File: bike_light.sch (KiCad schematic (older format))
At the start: 0 parts

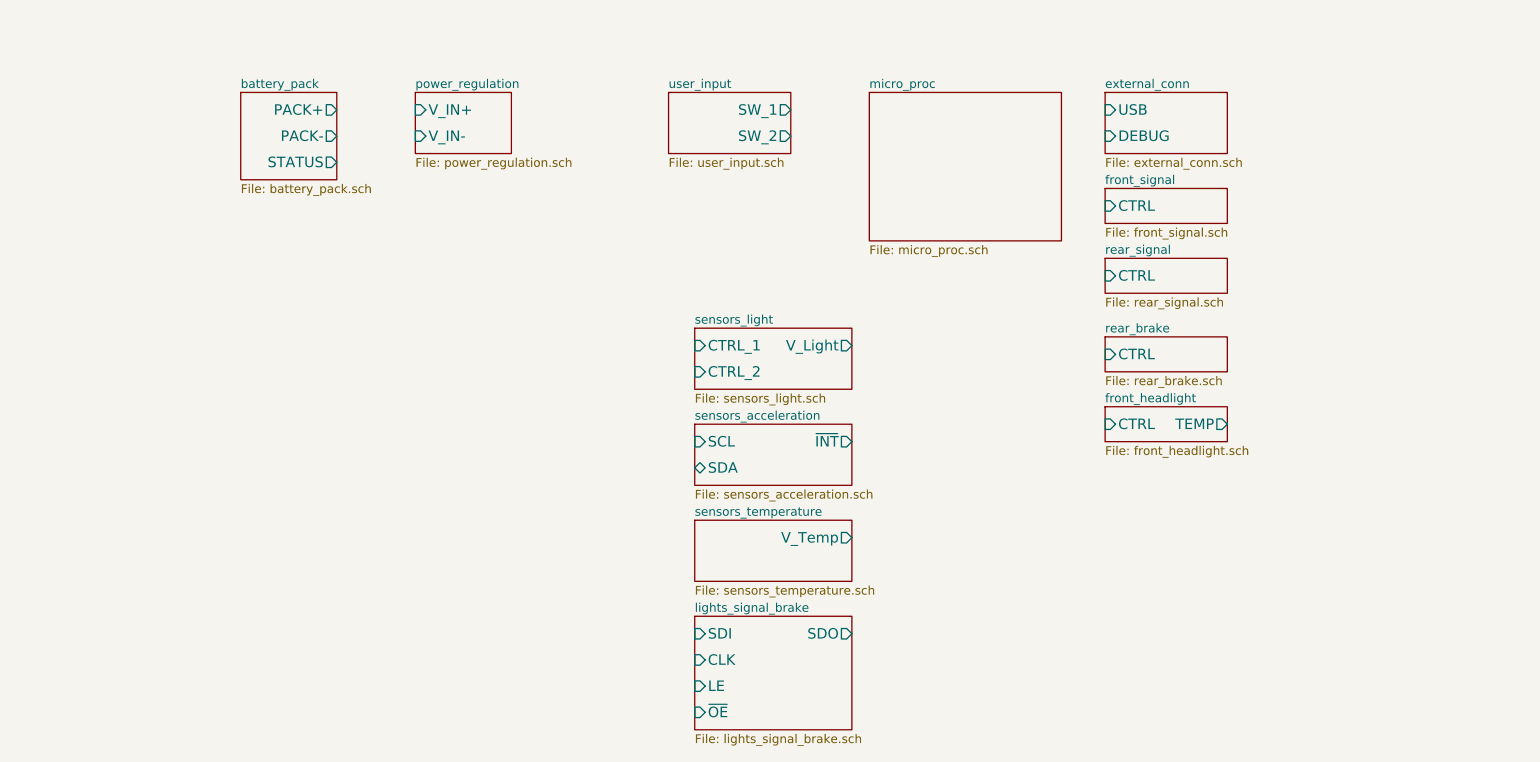
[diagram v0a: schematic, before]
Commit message: Various components added
USB conn, general outputs, brake signal, touch sensor
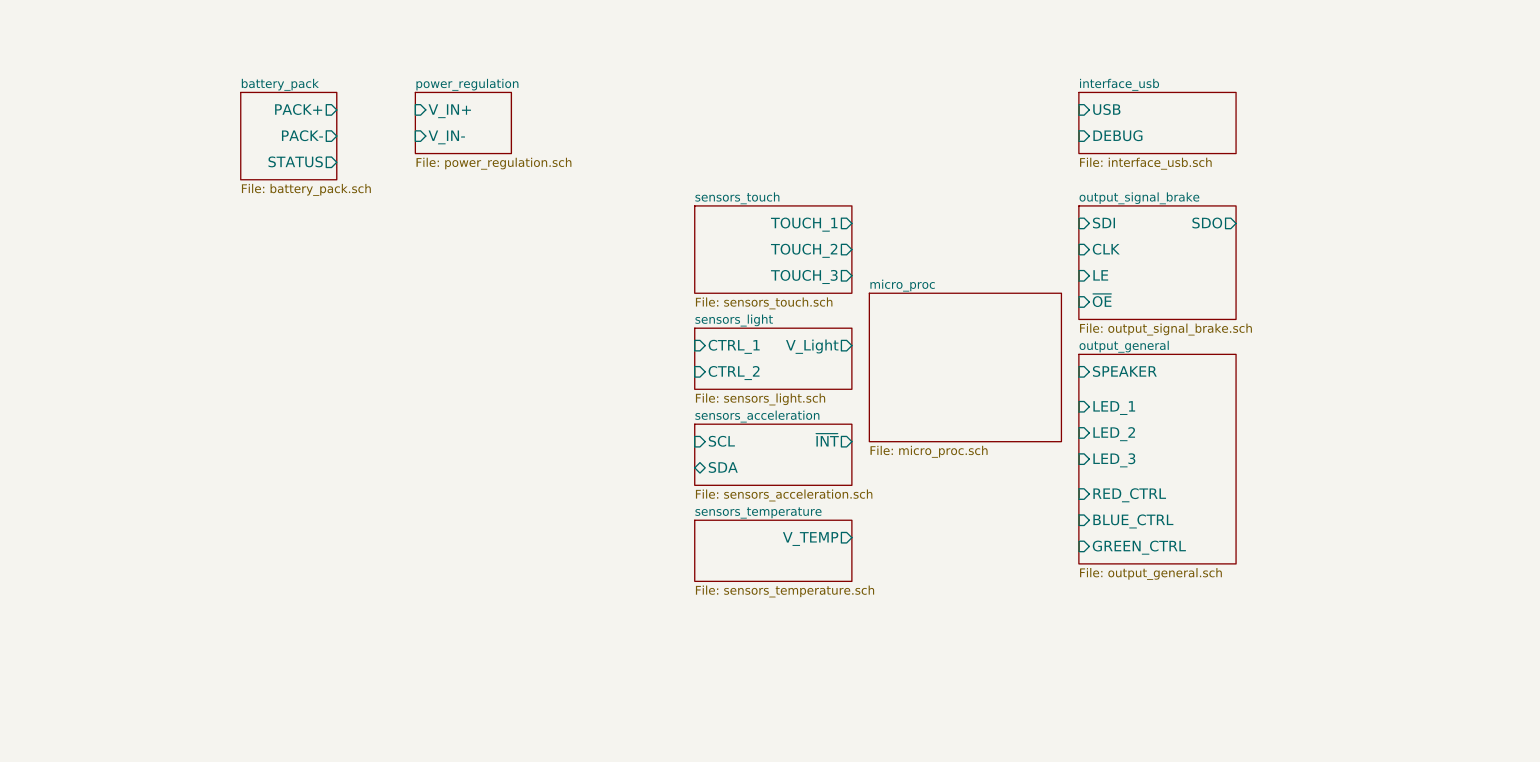
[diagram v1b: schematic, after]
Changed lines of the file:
@@
 $Descr USLetter 11000 8500
 encoding utf-8
-Sheet 1 14
+Sheet 1 11
 Title "Bike Light"
-Date "10 nov 2013"
+Date "11 nov 2013"
 Rev "1.0"
 Comp ""
@@
 $EndSheet
 $Sheet
-S 5500 1100 1100 850
+S 5500 2250 1100 850
 U 5224C543
 F0 "micro_proc" 50
@@
 $EndSheet
 $Sheet
-S 4350 1100 700  350
-U 5224C574
-F0 "user_input" 50
-F1 "user_input.sch" 50
-F2 "SW_1" O R 5050 1200 60
-F3 "SW_2" O R 5050 1350 60
-$EndSheet
-$Sheet
-S 6850 1100 700  350
+S 6700 1100 900  350
 U 5224C595
-F0 "external_conn" 50
-F1 "external_conn.sch" 50
-F2 "USB" I L 6850 1200 60
-F3 "DEBUG" I L 6850 1350 60
-$EndSheet
-$Sheet
-S 6850 2500 700  200
-U 5224C62E
-F0 "rear_brake" 50
-F1 "rear_brake.sch" 50
-F2 "CTRL" I L 6850 2600 60
-$EndSheet
-$Sheet
-S 6850 2050 700  200
-U 5224C648
-F0 "rear_signal" 50
-F1 "rear_signal.sch" 50
-F2 "CTRL" I L 6850 2150 60
-$EndSheet
-$Sheet
-S 6850 2900 700  200
-U 5224C659
-F0 "front_headlight" 50
-F1 "front_headlight.sch" 50
-F2 "CTRL" I L 6850 3000 60
-F3 "TEMP" O R 7550 3000 60
-$EndSheet
-$Sheet
-S 6850 1650 700  200
-U 5224C605
-F0 "front_signal" 50
-F1 "front_signal.sch" 50
-F2 "CTRL" I L 6850 1750 60
+F0 "interface_usb" 50
+F1 "interface_usb.sch" 50
+F2 "USB" I L 6700 1200 60
+F3 "DEBUG" I L 6700 1350 60
 $EndSheet
 $Sheet
@@
 F0 "sensors_temperature" 50
 F1 "sensors_temperature.sch" 50
-F2 "V_Temp" O R 5400 3650 60
+F2 "V_TEMP" O R 5400 3650 60
 $EndSheet
 $Sheet
@@
 $EndSheet
 $Sheet
-S 4500 4100 900  650
+S 6700 1750 900  650
 U 527F3E83
-F0 "lights_signal_brake" 50
-F1 "lights_signal_brake.sch" 50
-F2 "SDI" I L 4500 4200 60
-F3 "CLK" I L 4500 4350 60
-F4 "LE" I L 4500 4500 60
-F5 "~OE" I L 4500 4650 60
-F6 "SDO" O R 5400 4200 60
+F0 "output_signal_brake" 50
+F1 "output_signal_brake.sch" 50
+F2 "SDI" I L 6700 1850 60
+F3 "CLK" I L 6700 2000 60
+F4 "LE" I L 6700 2150 60
+F5 "~OE" I L 6700 2300 60
+F6 "SDO" O R 7600 1850 60
+$EndSheet
+$Sheet
+S 4500 1750 900  500
+U 527FE989
+F0 "sensors_touch" 50
+F1 "sensors_touch.sch" 50
+F2 "TOUCH_1" O R 5400 1850 60
+F3 "TOUCH_2" O R 5400 2000 60
+F4 "TOUCH_3" O R 5400 2150 60
+$EndSheet
+$Sheet
+S 6700 2600 900  1200
+U 528029D1
+F0 "output_general" 50
+F1 "output_general.sch" 50
+F2 "SPEAKER" I L 6700 2700 60
+F3 "LED_1" I L 6700 2900 60
+F4 "LED_2" I L 6700 3050 60
+F5 "LED_3" I L 6700 3200 60
+F6 "RED_CTRL" I L 6700 3400 60
+F7 "BLUE_CTRL" I L 6700 3550 60
+F8 "GREEN_CTRL" I L 6700 3700 60
 $EndSheet
 $EndSCHEMATC

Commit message: Battery management stuff
:D
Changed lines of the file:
@@
 $Descr USLetter 11000 8500
 encoding utf-8
-Sheet 1 11
+Sheet 1 14
 Title "Bike Light"
-Date "11 nov 2013"
+Date "12 nov 2013"
 Rev "1.0"
 Comp ""
@@
 $EndDescr
 $Sheet
-S 1900 1100 550  500
+S 2450 1650 1000 350
 U 5224C457
 F0 "battery_pack" 50
 F1 "battery_pack.sch" 50
-F2 "PACK+" O R 2450 1200 60
-F3 "PACK-" O R 2450 1350 60
-F4 "STATUS" O R 2450 1500 60
+F2 "V_PACK" O R 3450 1750 60
+F3 "V_PACK_BUFFERED" O R 3450 1900 60
 $EndSheet
 $Sheet
-S 2900 1100 550  350
+S 3850 850  550  350
 U 5224C4FA
 F0 "power_regulation" 50
 F1 "power_regulation.sch" 50
-F2 "V_IN-" I L 2900 1350 60
-F3 "V_IN+" I L 2900 1200 60
+F2 "V_IN-" I L 3850 1100 60
+F3 "V_IN+" I L 3850 950 60
 $EndSheet
 $Sheet
@@
 $EndSheet
 $Sheet
-S 4500 3550 900  350
+S 4500 3550 900  200
 U 527B19B4
 F0 "sensors_temperature" 50

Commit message: random minor thing
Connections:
- wire segments 0 -> 32
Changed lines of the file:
@@
 Sheet 1 14
 Title "Bike Light"
-Date "12 nov 2013"
+Date "15 nov 2013"
 Rev "1.0"
 Comp ""
@@
 $EndSheet
 $Sheet
-S 5500 2250 1100 850
+S 5500 1750 1100 2350
 U 5224C543
 F0 "micro_proc" 50
@@
 $EndSheet
 $Sheet
-S 6700 1100 900  350
+S 6700 750  900  350
 U 5224C595
 F0 "interface_usb" 50
 F1 "interface_usb.sch" 50
-F2 "USB" I L 6700 1200 60
-F3 "DEBUG" I L 6700 1350 60
+F2 "USB" I L 6700 850 60
+F3 "DEBUG" I L 6700 1000 60
 $EndSheet
 $Sheet
-S 4500 3550 900  200
+S 4500 3750 900  200
 U 527B19B4
 F0 "sensors_temperature" 50
 F1 "sensors_temperature.sch" 50
-F2 "V_TEMP" O R 5400 3650 60
+F2 "V_TEMP" O R 5400 3850 60
 $EndSheet
 $Sheet
-S 4500 2450 900  350
+S 4500 2550 900  350
 U 527B1CA6
 F0 "sensors_light" 50
 F1 "sensors_light.sch" 50
-F2 "V_Light" O R 5400 2550 60
-F3 "CTRL_1" I L 4500 2550 60
-F4 "CTRL_2" I L 4500 2700 60
+F2 "V_Light" O R 5400 2650 60
+F3 "CTRL_1" I L 4500 2650 60
+F4 "CTRL_2" I L 4500 2800 60
 $EndSheet
 $Sheet
-S 4500 3000 900  350
+S 4500 3200 900  350
 U 527C7E4B
 F0 "sensors_acceleration" 50
 F1 "sensors_acceleration.sch" 50
-F2 "SCL" I L 4500 3100 60
-F3 "SDA" B L 4500 3250 60
-F4 "~INT" O R 5400 3100 60
+F2 "SCL" I L 4500 3300 60
+F3 "SDA" B L 4500 3450 60
+F4 "~INT" O R 5400 3300 60
 $EndSheet
 $Sheet
@@
 F8 "GREEN_CTRL" I L 6700 3700 60
 $EndSheet
+Wire Wire Line
+	5400 1850 5500 1850
+Wire Wire Line
+	5400 2000 5500 2000
+Wire Wire Line
+	5400 2150 5500 2150
+Wire Wire Line
+	4500 2650 4450 2650
+Wire Wire Line
+	4450 2650 4450 2450
+Wire Wire Line
+	4450 2450 5500 2450
+Wire Wire Line
+	4500 2800 4350 2800
+Wire Wire Line
+	4350 2800 4350 2350
+Wire Wire Line
+	4350 2350 5500 2350
+Wire Wire Line
+	5400 2650 5500 2650
+Wire Wire Line
+	4500 3300 4450 3300
+Wire Wire Line
+	4450 3300 4450 3100
+Wire Wire Line
+	4450 3100 5500 3100
+Wire Wire Line
+	4500 3450 4350 3450
+Wire Wire Line
+	4350 3450 4350 3000
+Wire Wire Line
+	4350 3000 5500 3000
+Wire Wire Line
+	5400 3300 5500 3300
+Wire Wire Line
+	5400 3850 5500 3850
+Wire Wire Line
+	6600 1850 6700 1850
+Wire Wire Line
+	6700 2000 6600 2000
+Wire Wire Line
+	6700 2150 6600 2150
+Wire Wire Line
+	6700 2300 6600 2300
+Wire Wire Line
+	7600 1850 7850 1850
+Wire Wire Line
+	7850 1850 7850 2500
+Wire Wire Line
+	7850 2500 6600 2500
+Wire Wire Line
+	6700 2700 6600 2700
+Wire Wire Line
+	6700 2900 6600 2900
+Wire Wire Line
+	6700 3050 6600 3050
+Wire Wire Line
+	6700 3200 6600 3200
+Wire Wire Line
+	6700 3400 6600 3400
+Wire Wire Line
+	6700 3550 6600 3550
+Wire Wire Line
+	6700 3700 6600 3700
 $EndSCHEMATC

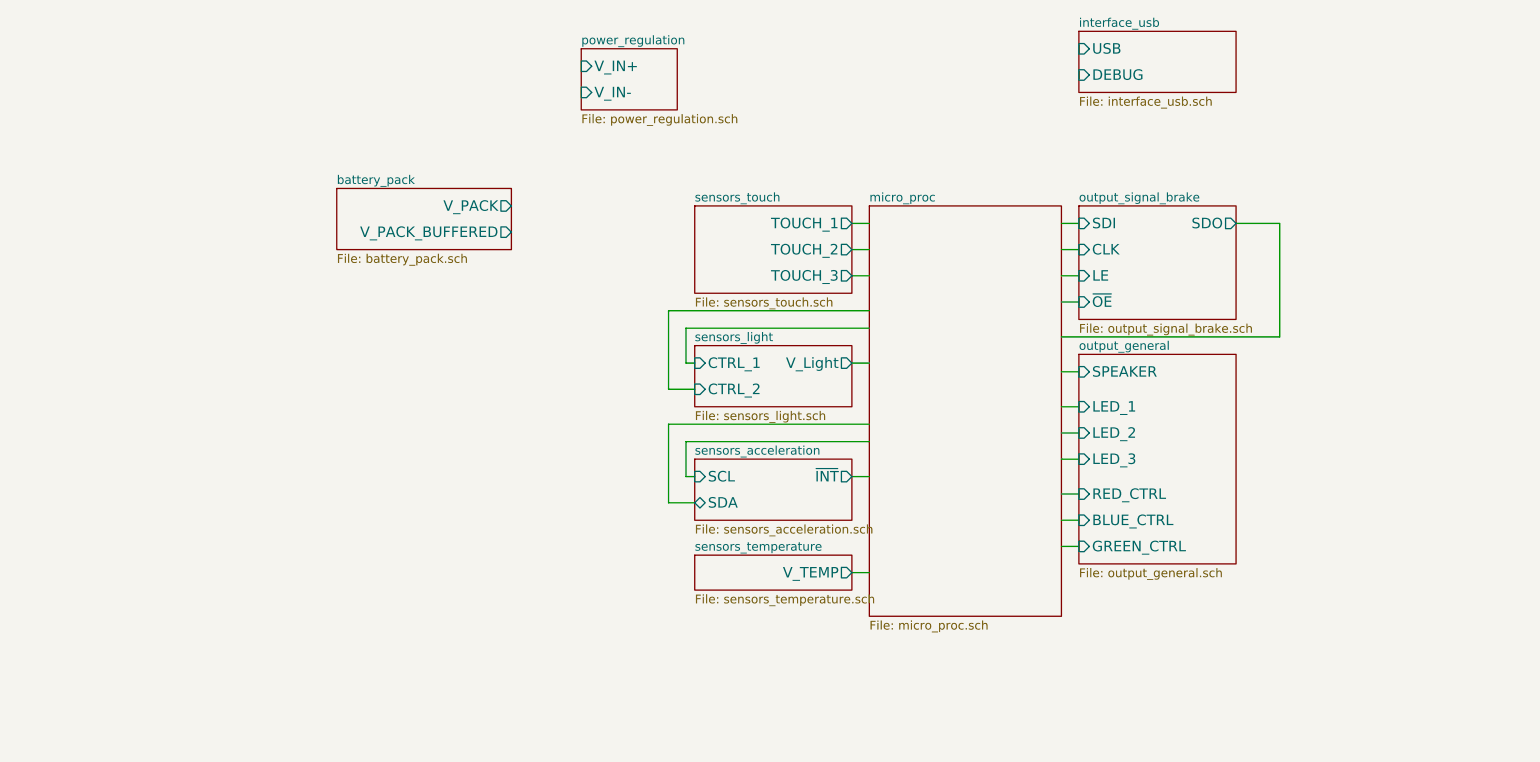
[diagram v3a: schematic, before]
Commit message: Added comments to schematic
shows what needs to be done
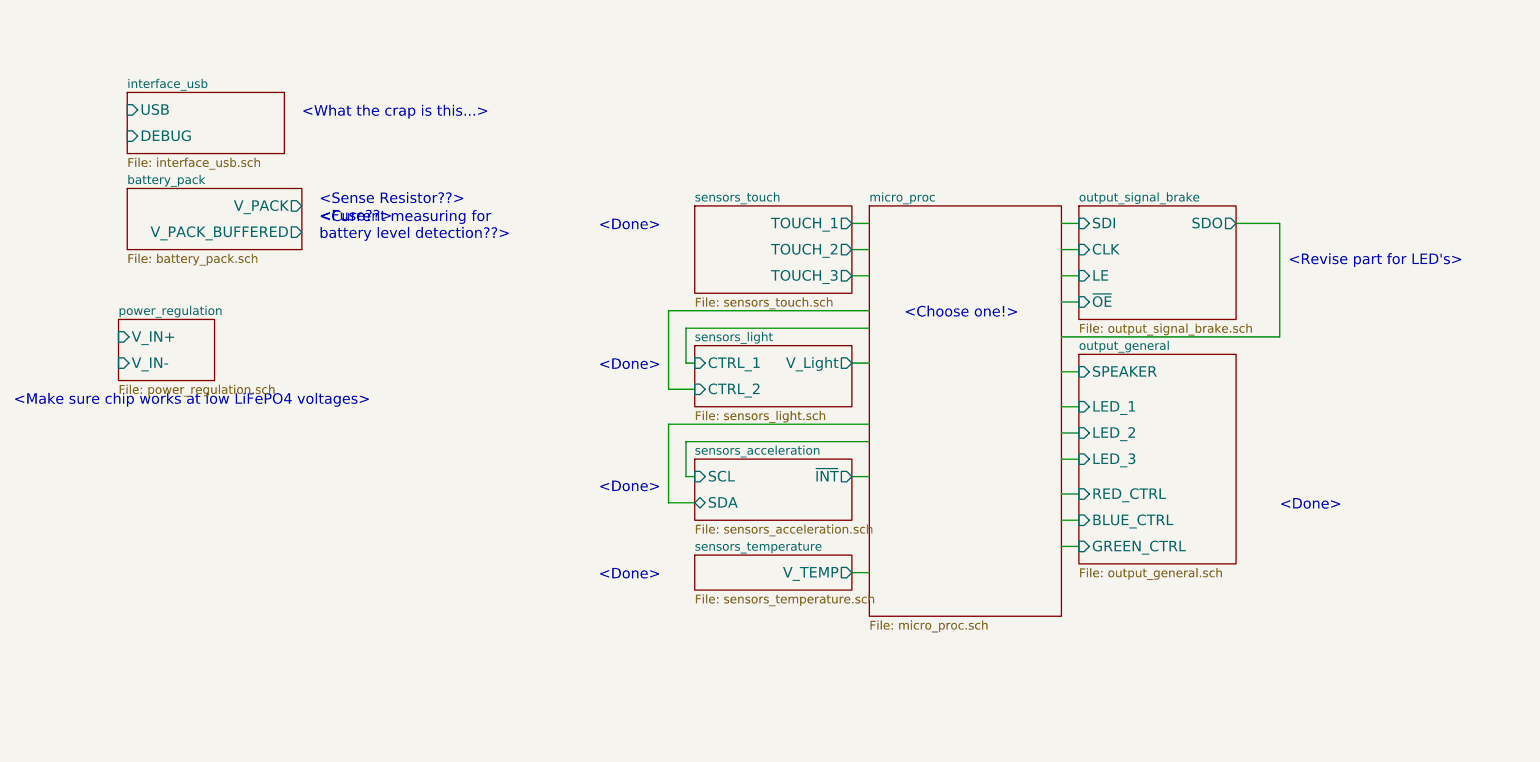
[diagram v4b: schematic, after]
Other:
- note added: "<Choose one!>"
- note added: "<Current measuring for \nbattery level detection??>"
- note added: "<Done>"
- note added: "<Fuse??>"
- note added: "<Make sure chip works at low LiFePO4 voltages>"
- note added: "<Revise part for LED's>"
- note added: "<Sense Resistor??>"
- note added: "<What the crap is this...>"
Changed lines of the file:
@@
 Sheet 1 14
 Title "Bike Light"
-Date "15 nov 2013"
+Date "17 nov 2013"
 Rev "1.0"
 Comp ""
@@
 $EndDescr
 $Sheet
-S 2450 1650 1000 350
+S 1250 1650 1000 350
 U 5224C457
 F0 "battery_pack" 50
 F1 "battery_pack.sch" 50
-F2 "V_PACK" O R 3450 1750 60
-F3 "V_PACK_BUFFERED" O R 3450 1900 60
+F2 "V_PACK" O R 2250 1750 60
+F3 "V_PACK_BUFFERED" O R 2250 1900 60
 $EndSheet
 $Sheet
-S 3850 850  550  350
+S 1200 2400 550  350
 U 5224C4FA
 F0 "power_regulation" 50
 F1 "power_regulation.sch" 50
-F2 "V_IN-" I L 3850 1100 60
-F3 "V_IN+" I L 3850 950 60
+F2 "V_IN-" I L 1200 2650 60
+F3 "V_IN+" I L 1200 2500 60
 $EndSheet
 $Sheet
@@
 $EndSheet
 $Sheet
-S 6700 750  900  350
+S 1250 1100 900  350
 U 5224C595
 F0 "interface_usb" 50
 F1 "interface_usb.sch" 50
-F2 "USB" I L 6700 850 60
-F3 "DEBUG" I L 6700 1000 60
+F2 "USB" I L 1250 1200 60
+F3 "DEBUG" I L 1250 1350 60
 $EndSheet
 $Sheet
@@
 Wire Wire Line
 	6700 3700 6600 3700
+Text Notes 3950 1900 0    60   ~ 0
+<Done>
+Text Notes 3950 2700 0    60   ~ 0
+<Done>
+Text Notes 3950 3900 0    60   ~ 0
+<Done>
+Text Notes 7850 3500 0    60   ~ 0
+<Done>
+Text Notes 7900 2100 0    60   ~ 0
+<Revise part for LED's>
+Text Notes 5700 2400 0    60   ~ 0
+<Choose one!>
+Text Notes 3950 3400 0    60   ~ 0
+<Done>
+Text Notes 2350 1750 0    60   ~ 0
+<Sense Resistor??>
+Text Notes 2350 1850 0    60   ~ 0
+<Fuse??>
+Text Notes 2350 1950 0    60   ~ 0
+<Current measuring for \nbattery level detection??>
+Text Notes 2250 1250 0    60   ~ 0
+<What the crap is this...>
+Text Notes 600  2900 0    60   ~ 0
+<Make sure chip works at low LiFePO4 voltages>
 $EndSCHEMATC

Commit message: revised LED parts to match reality
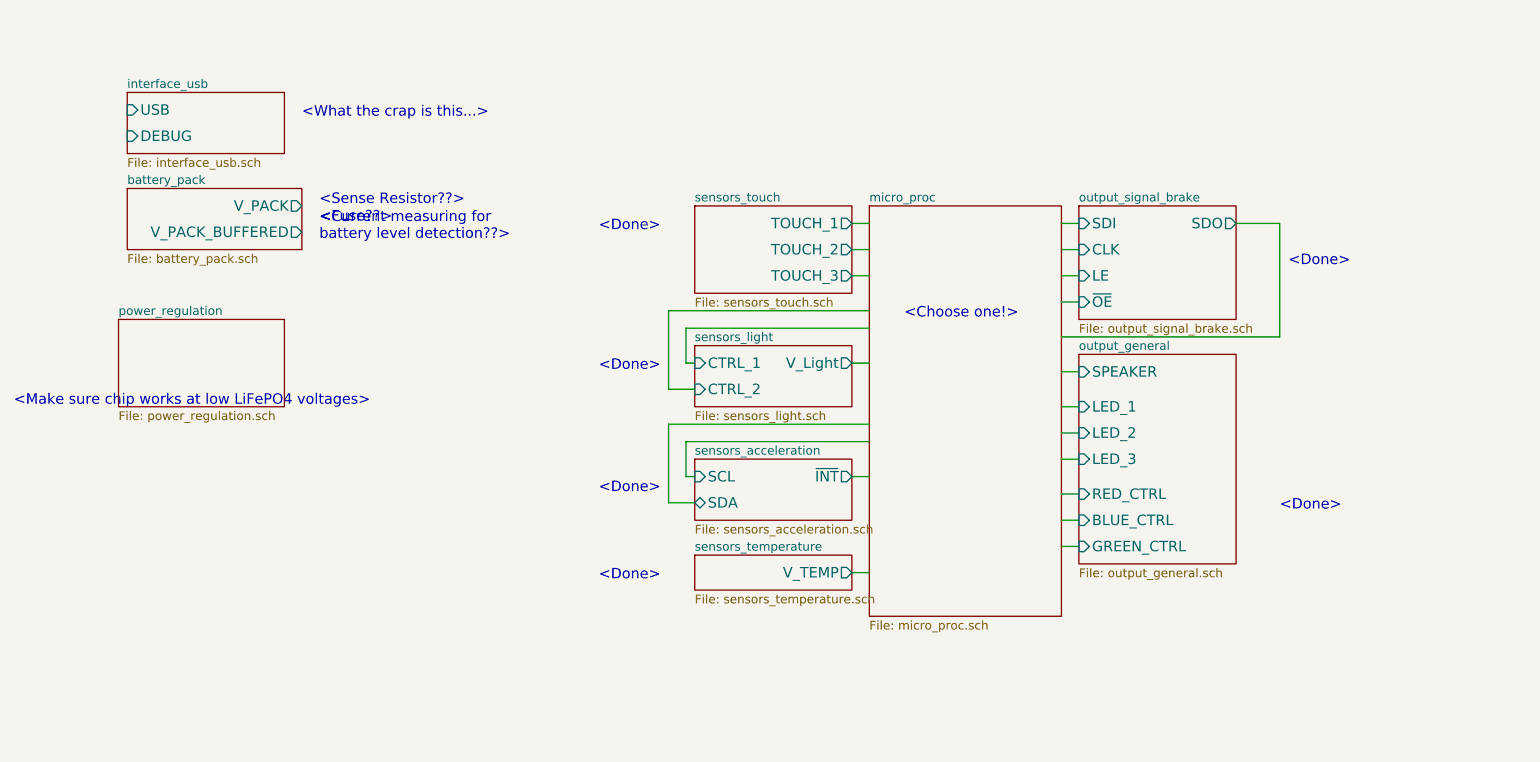
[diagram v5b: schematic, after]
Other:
- note removed: "<Revise part for LED's>"
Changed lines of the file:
@@
 Sheet 1 14
 Title "Bike Light"
-Date "17 nov 2013"
+Date "18 nov 2013"
 Rev "1.0"
 Comp ""
@@
 $EndSheet
 $Sheet
-S 1200 2400 550  350
+S 1200 2400 950  500
 U 5224C4FA
 F0 "power_regulation" 50
 F1 "power_regulation.sch" 50
-F2 "V_IN-" I L 1200 2650 60
-F3 "V_IN+" I L 1200 2500 60
 $EndSheet
 $Sheet
@@
 <Done>
 Text Notes 7900 2100 0    60   ~ 0
-<Revise part for LED's>
+<Done>
 Text Notes 5700 2400 0    60   ~ 0
 <Choose one!>
